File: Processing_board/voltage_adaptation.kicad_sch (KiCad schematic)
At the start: 17 parts, among them Q1 DMP3056LSS-13, U2 TPS7A7200RGW, U6 LD1117S33TR_SOT223

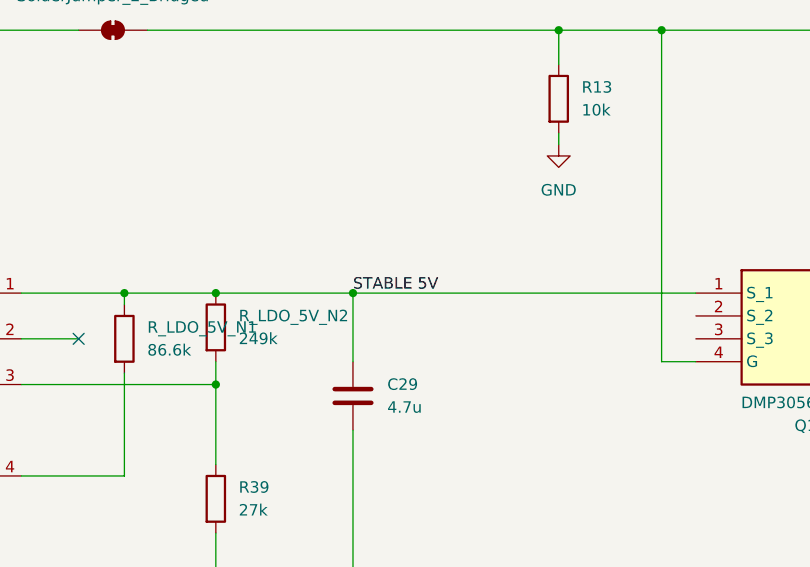
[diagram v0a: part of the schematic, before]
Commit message: fix: changed back silkscreen
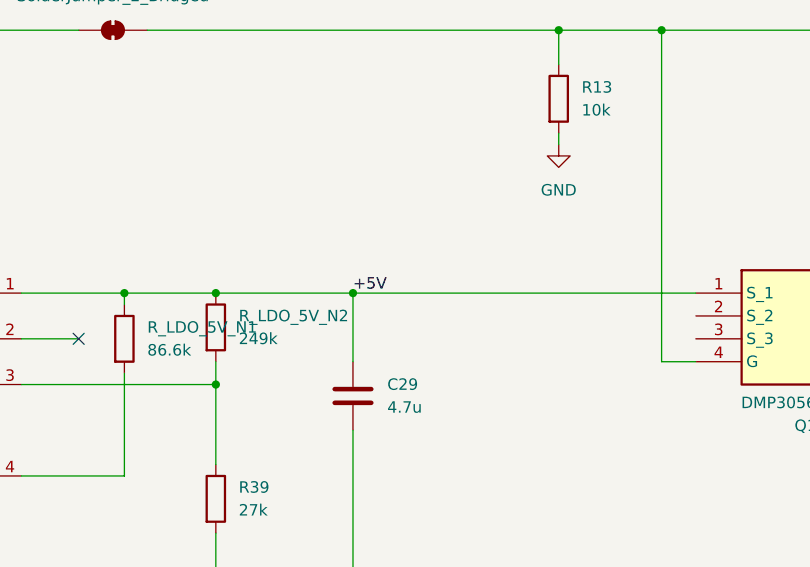
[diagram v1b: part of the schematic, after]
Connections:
- net STABLE 5V renamed +5V
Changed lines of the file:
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@@
 		)
 	)
-	(label "STABLE 5V"
+	(label "+5V"
 		(at 128.27 81.28 0)
 		(effects
